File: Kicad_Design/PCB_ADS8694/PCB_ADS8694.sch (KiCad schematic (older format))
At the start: 46 parts, among them J1 Screw_Terminal_01x03_Alimenta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, J4 Conn_02x06_Male_Pmod_Spartan6, J5 Screw_Terminal_01x02_CH3, J6 Screw_Terminal_01x02_CH2, J7 Screw_Terminal_01x02_CH1, J8 Screw_Terminal_01x02_CH0, U1 LM7805_TO220, U2 AD8221, U3 AD8221, U4 ADS8694_Vers2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

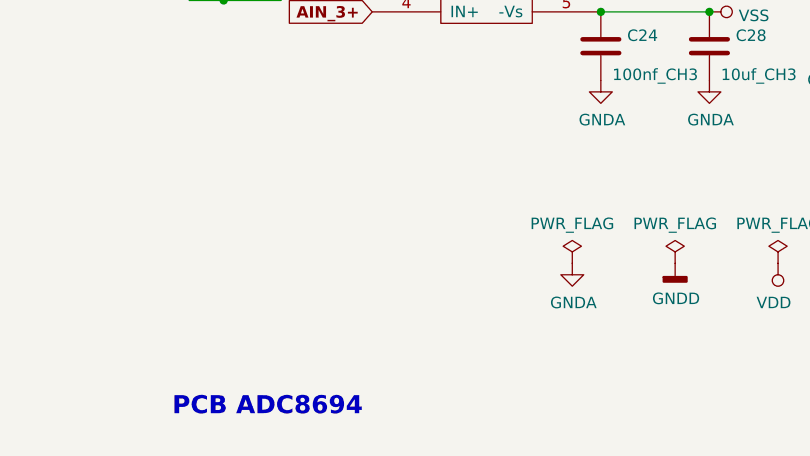
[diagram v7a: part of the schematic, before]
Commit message: Se cambia orientacion de bornera +-12V, con esto se evita usar vias para unir plano agnd. Se agregan vias para unir agnd con dgnd
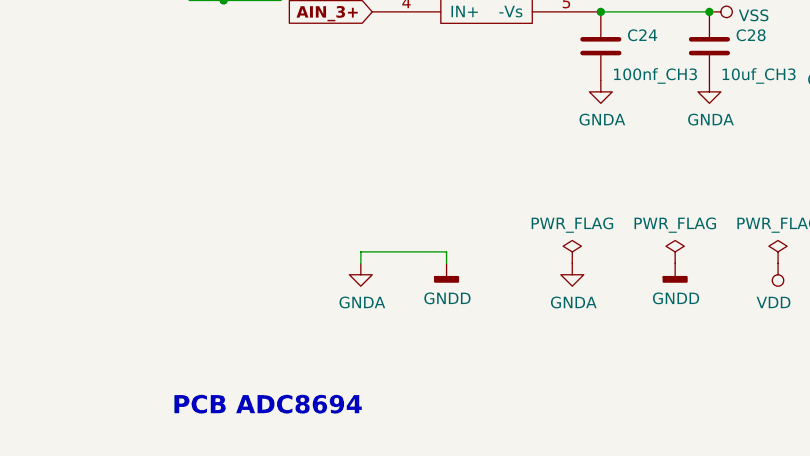
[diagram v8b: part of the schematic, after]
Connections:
- net GNDD is gone; now on net GNDA: C4.1, J4.10 (Pin_10), J4.9 (Pin_9), U4.3 (DAISY), U4.33 (DGND)
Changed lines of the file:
@@
 Wire Wire Line
 	2500 1000 2500 1050
-Text GLabel 6250 4400 2    50   Input ~ 6
+Text GLabel 6250 4400 2    50   Input ~ 10
 REFSEL
-Text GLabel 6250 4700 2    50   Input ~ 6
+Text GLabel 6250 4700 2    50   Input ~ 10
 ALARM
-Text GLabel 6250 4900 2    50   Input ~ 6
+Text GLabel 6250 4900 2    50   Input ~ 10
 REFCAP
-Text GLabel 6250 5100 2    50   Input ~ 6
+Text GLabel 6250 5100 2    50   Input ~ 10
 REFIO
-Text GLabel 6250 4200 2    50   Input ~ 6
+Text GLabel 6250 4200 2    50   Input ~ 10
 RST-PD
-Text GLabel 6250 3900 2    50   Input ~ 6
+Text GLabel 6250 3900 2    50   Input ~ 10
 CS
-Text GLabel 6250 3800 2    50   Input ~ 6
+Text GLabel 6250 3800 2    50   Input ~ 10
 SCLK
-Text GLabel 6250 3700 2    50   Input ~ 6
+Text GLabel 6250 3700 2    50   Input ~ 10
 SDI
-Text GLabel 6250 3600 2    50   Input ~ 6
+Text GLabel 6250 3600 2    50   Input ~ 10
 SDO
-Text GLabel 5250 3800 0    50   Input ~ 6
+Text GLabel 5250 3800 0    50   Input ~ 10
 AIN_1P
-Text GLabel 5250 4000 0    50   Input ~ 6
+Text GLabel 5250 4000 0    50   Input ~ 10
 AIN_2P
-Text GLabel 5250 4200 0    50   Input ~ 6
+Text GLabel 5250 4200 0    50   Input ~ 10
 AIN_3P
-Text GLabel 7200 800  0    50   Input ~ 6
+Text GLabel 7200 800  0    50   Input ~ 10
 REFSEL
-Text GLabel 7200 1150 0    50   Input ~ 6
+Text GLabel 7200 1150 0    50   Input ~ 10
 REFIO
-Text GLabel 7200 1550 0    50   Input ~ 6
+Text GLabel 7200 1550 0    50   Input ~ 10
 REFCAP
 Wire Wire Line
 	7200 1550 7200 1950
-Text Notes 6750 2650 0    50   ~ 6
+Text Notes 6750 2650 0    50   ~ 10
 CONFIGURACIÓN PARA USAR\nREFERENCIA INTERNA 4.096 [V]\n
-Text Notes 4950 1675 0    50   ~ 6
+Text Notes 4950 1675 0    50   ~ 10
 PMOD FPGA
 Wire Notes Line
@@
 Wire Notes Line
 	2950 650  950  650
-Text Notes 1450 1750 0    50   ~ 6
+Text Notes 1450 1750 0    50   ~ 10
 REGULADOR DE TENSIÓN, 5V\n
-Text Notes 7450 7500 0    79   ~ 6
+Text Notes 7450 7500 0    79   ~ 16
 PCB ADC8694
 Wire Notes Line
 	950  650  950  1800
-Text GLabel 4900 1275 0    50   Input ~ 6
+Text GLabel 4900 1275 0    50   Input ~ 10
 SCLK
-Text GLabel 4900 1475 0    50   Input ~ 6
+Text GLabel 4900 1475 0    50   Input ~ 10
 SDO
-Text GLabel 4900 1175 0    50   Input ~ 6
+Text GLabel 4900 1175 0    50   Input ~ 10
 SDI
 Wire Notes Line
 	6200 650  4150 650
-Text Notes 1400 2700 0    50   ~ 6
+Text Notes 1400 2700 0    50   ~ 10
 FUENTE DE CC EXTERNA, +-VCC
 Wire Notes Line
@@
 	1    0    0    -1
 $EndComp
-Text GLabel 9200 3425 2    50   Input ~ 6
+Text GLabel 9200 3425 2    50   Input ~ 10
 AIN_0P
-Text GLabel 8200 3625 0    50   Input ~ 6
+Text GLabel 8200 3625 0    50   Input ~ 10
 AIN_0+
-Text GLabel 8200 3325 0    50   Input ~ 6
+Text GLabel 8200 3325 0    50   Input ~ 10
 AIN_0-
 $Comp
@@
 	0    1    1    0
 $EndComp
-Text GLabel 8325 5425 0    50   Input ~ 6
+Text GLabel 8325 5425 0    50   Input ~ 10
 AIN_3-
-Text GLabel 8325 5725 0    50   Input ~ 6
+Text GLabel 8325 5725 0    50   Input ~ 10
 AIN_3+
 Connection ~ 1125 6750
@@
 	0    1    1    0
 $EndComp
-Text GLabel 1775 6500 0    50   Input ~ 6
+Text GLabel 1775 6500 0    50   Input ~ 10
 AIN_2-
-Text GLabel 1775 6800 0    50   Input ~ 6
+Text GLabel 1775 6800 0    50   Input ~ 10
 AIN_2+
 Connection ~ 1025 5175
@@
 	0    1    1    0
 $EndComp
-Text GLabel 1675 4925 0    50   Input ~ 6
+Text GLabel 1675 4925 0    50   Input ~ 10
 AIN_1-
-Text GLabel 1675 5225 0    50   Input ~ 6
+Text GLabel 1675 5225 0    50   Input ~ 10
 AIN_1+
 $Comp
@@
 	1    0    0    -1
 $EndComp
-Text Notes 8100 4375 0    50   ~ 6
+Text Notes 8100 4375 0    50   ~ 10
 ENTRADA CON ACONDICIONAMIENTO SIN FILTRO RC\n
-Text Notes 1275 4175 0    50   ~ 6
+Text Notes 1275 4175 0    50   ~ 10
 CONECTORES DE ENTRADA DE SEÑAL
 $Comp
@@
 	1    0    0    -1
 $EndComp
-Text GLabel 2500 1000 2    50   Input ~ 6
+Text GLabel 2500 1000 2    50   Input ~ 10
 AVDD
-Text GLabel 5650 3100 1    50   Input ~ 6
+Text GLabel 5650 3100 1    50   Input ~ 10
 AVDD
 $Comp
@@
 Wire Wire Line
 	4600 3700 4600 3900
-Text GLabel 5250 3600 0    50   Input ~ 6
+Text GLabel 5250 3600 0    50   Input ~ 10
 AIN_0P
 $Comp
@@
 	0    1    1    0
 $EndComp
-Text GLabel 3900 5025 2    50   Input ~ 6
+Text GLabel 3900 5025 2    50   Input ~ 10
 AIN_1P
 $Comp
@@
 	0    1    1    0
 $EndComp
-Text GLabel 4000 6600 2    50   Input ~ 6
+Text GLabel 4000 6600 2    50   Input ~ 10
 AIN_2P
 $Comp
@@
 	0    1    1    0
 $EndComp
-Text GLabel 10550 5525 2    50   Input ~ 6
+Text GLabel 10550 5525 2    50   Input ~ 10
 AIN_3P
 $Comp
@@
 	1    0    0    -1
 $EndComp
-Text GLabel 5750 3100 1    50   Input ~ 6
+Text GLabel 5750 3100 1    50   Input ~ 10
 AVDD
 $Comp
@@
 	-1   0    0    1
 $EndComp
-Text GLabel 3950 3050 1    50   Input ~ 6
+Text GLabel 3950 3050 1    50   Input ~ 10
 AVDD
 Wire Wire Line
@@
 Wire Notes Line
 	1250 2850 1250 4225
-Text GLabel 1850 3225 2    50   Input ~ 6
+Text GLabel 1850 3225 2    50   Input ~ 10
 AIN_3+
-Text GLabel 1850 3325 2    50   Input ~ 6
+Text GLabel 1850 3325 2    50   Input ~ 10
 AIN_3-
-Text GLabel 1850 3450 2    50   Input ~ 6
+Text GLabel 1850 3450 2    50   Input ~ 10
 AIN_2+
-Text GLabel 1850 3550 2    50   Input ~ 6
+Text GLabel 1850 3550 2    50   Input ~ 10
 AIN_2-
-Text GLabel 1850 3675 2    50   Input ~ 6
+Text GLabel 1850 3675 2    50   Input ~ 10
 AIN_1+
-Text GLabel 1850 3775 2    50   Input ~ 6
+Text GLabel 1850 3775 2    50   Input ~ 10
 AIN_1-
-Text GLabel 1850 3900 2    50   Input ~ 6
+Text GLabel 1850 3900 2    50   Input ~ 10
 AIN_0+
-Text GLabel 1850 4000 2    50   Input ~ 6
+Text GLabel 1850 4000 2    50   Input ~ 10
 AIN_0-
-Text Notes 1475 7575 0    50   ~ 6
+Text Notes 1475 7575 0    50   ~ 10
 ACONDICIONAMIENTO CON FILTRO PASA BAJO RC
 Wire Notes Line
@@
 Wire Wire Line
 	6825 4000 6250 4000
-Text GLabel 4900 975  0    50   Input ~ 6
+Text GLabel 4900 975  0    50   Input ~ 10
 RST-PD
-Text GLabel 5400 1075 2    50   Input ~ 6
+Text GLabel 5400 1075 2    50   Input ~ 10
 ALARM
-Text GLabel 4900 1075 0    50   Input ~ 6
+Text GLabel 4900 1075 0    50   Input ~ 10
 CS
 $Comp
@@
 Wire Notes Line
 	6200 1750 6200 650
+$Comp
+L power:GNDA #PWR?
+U 1 1 5CE84135
+P 8275 6825
+F 0 "#PWR?" H 8275 6575 50  0001 C CNN
+F 1 "GNDA" H 8280 6652 50  0000 C CNN
+F 2 "" H 8275 6825 50  0001 C CNN
+F 3 "" H 8275 6825 50  0001 C CNN
+	1    8275 6825
+	1    0    0    -1
+$EndComp
+$Comp
+L power:GNDD #PWR?
+U 1 1 5CE84736
+P 8650 6825
+F 0 "#PWR?" H 8650 6575 50  0001 C CNN
+F 1 "GNDD" H 8654 6670 50  0000 C CNN
+F 2 "" H 8650 6825 50  0001 C CNN
+F 3 "" H 8650 6825 50  0001 C CNN
+	1    8650 6825
+	1    0    0    -1
+$EndComp
+Wire Wire Line
+	8275 6825 8275 6775
+Wire Wire Line
+	8275 6775 8650 6775
+Wire Wire Line
+	8650 6775 8650 6825
 $EndSCHEMATC
